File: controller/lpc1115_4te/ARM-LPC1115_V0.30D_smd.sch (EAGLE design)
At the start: 97 parts, among them IC1 LPC1115, IC2 BD9G101, Q2 BCP52, Q3 BC856, Q4 12MHz, T1 BC547C

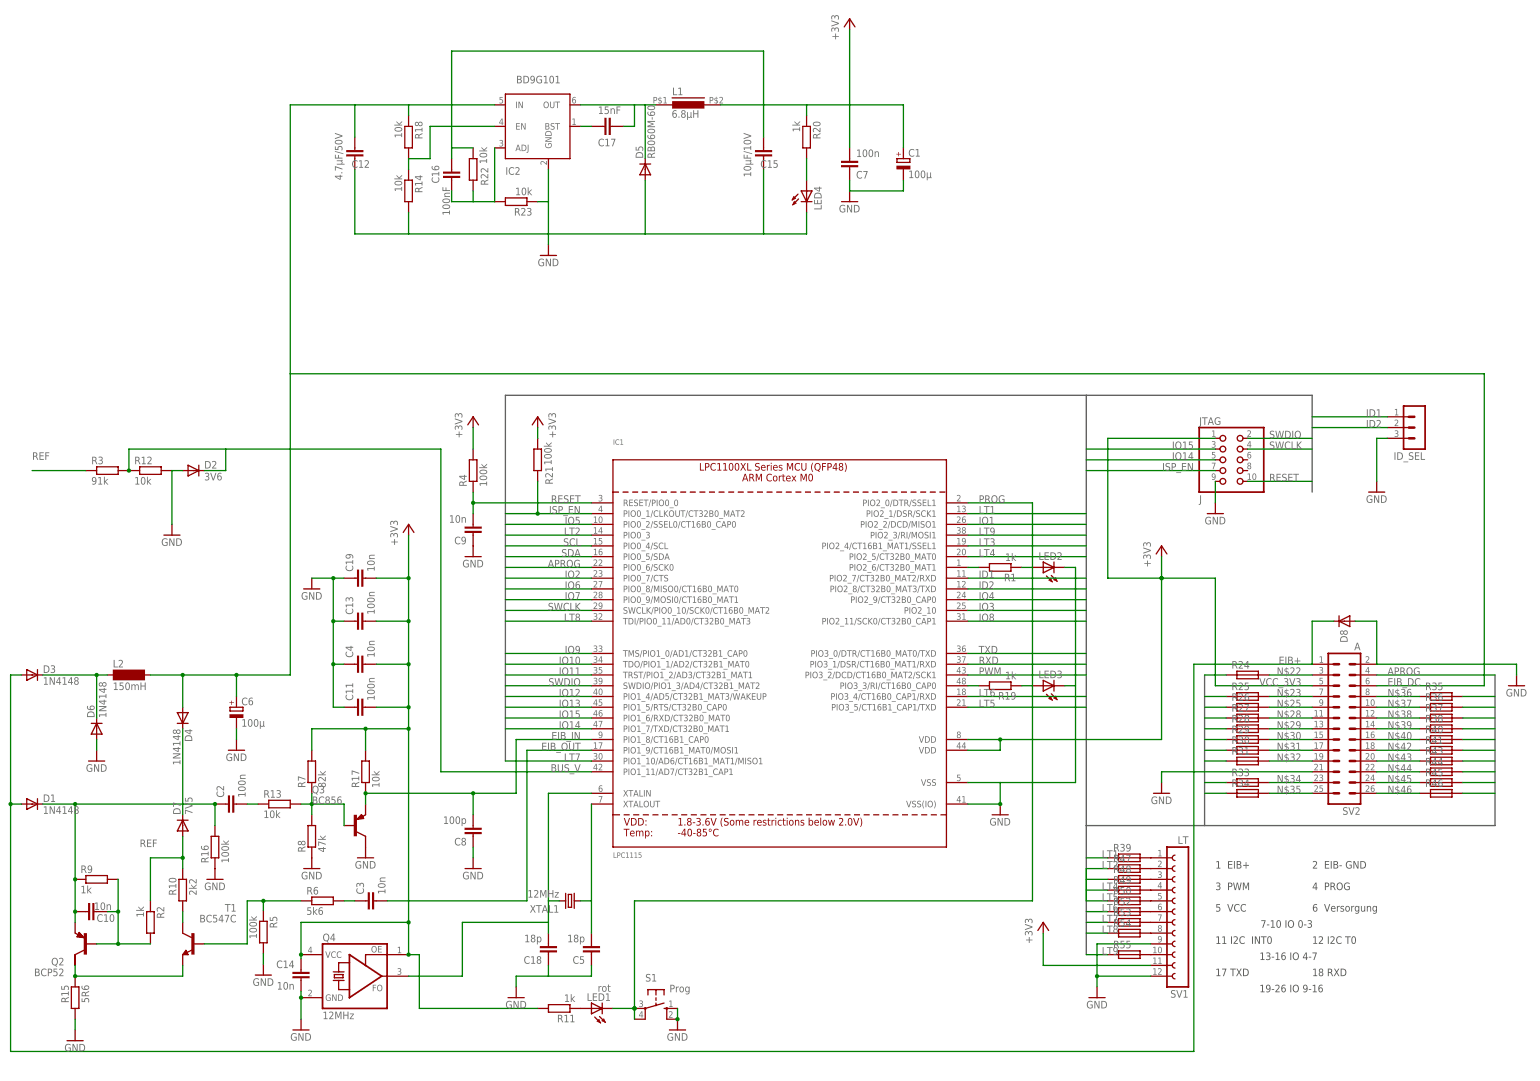
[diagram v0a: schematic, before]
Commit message: Bezeichungen verschoben und Hinweise ergänzt
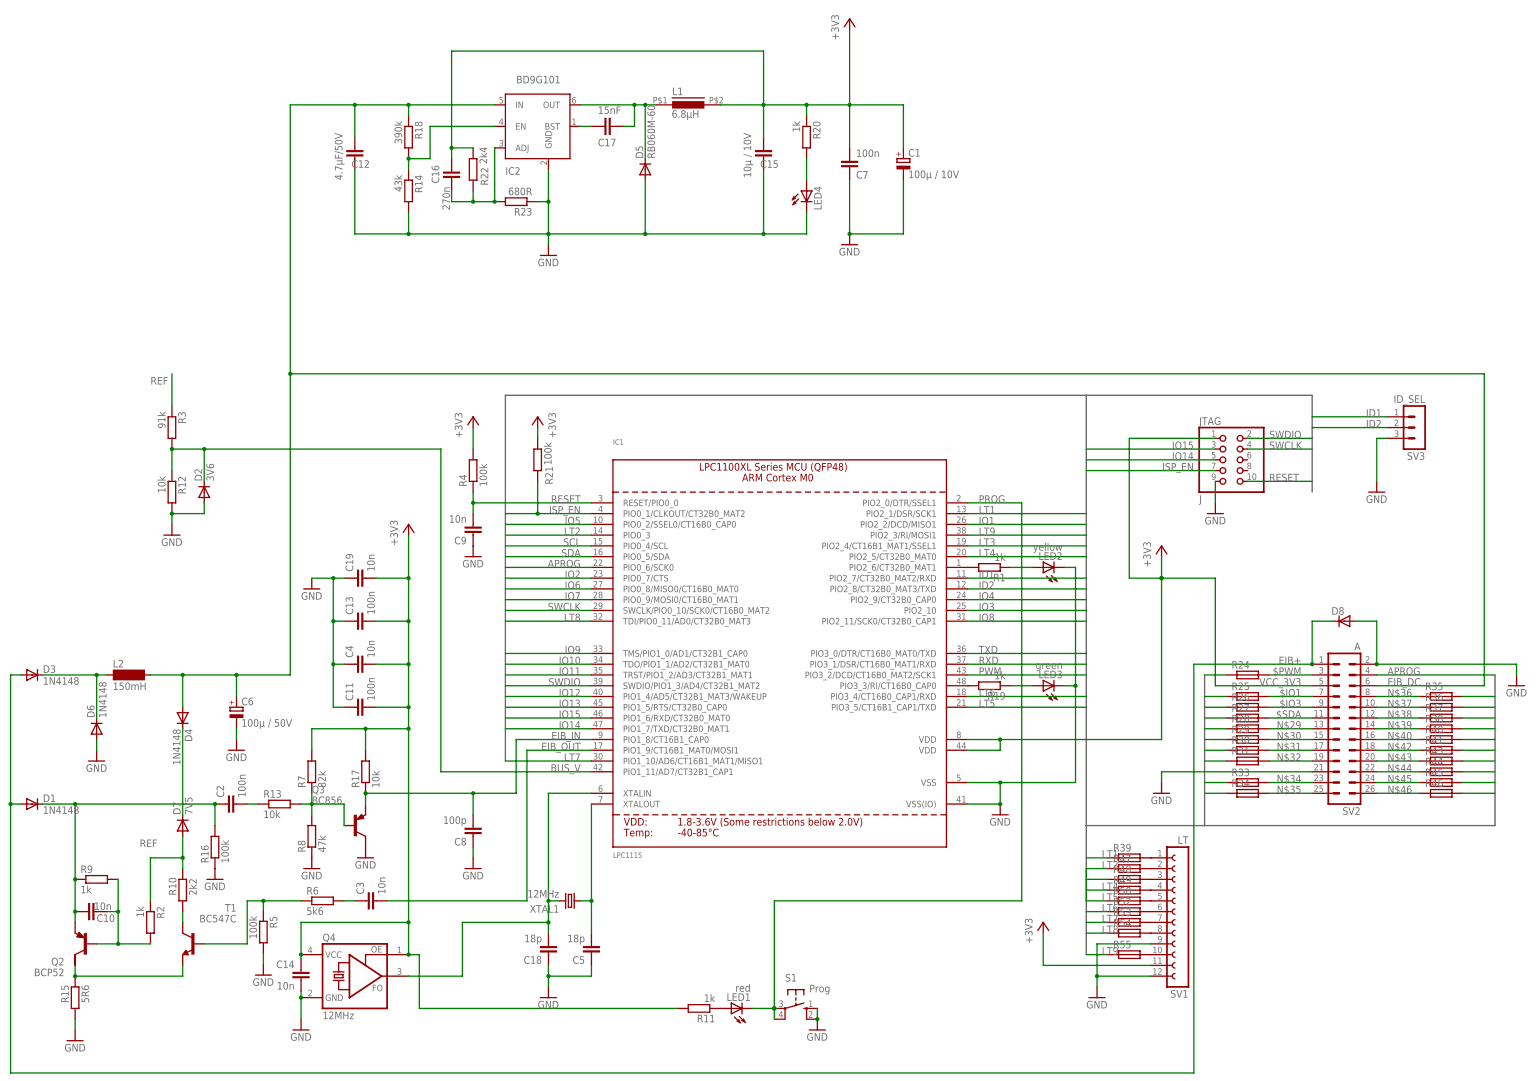
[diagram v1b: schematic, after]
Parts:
- C1: value 100µ -> 100µ / 10V
- C15: value 10µF/10V -> 10µ / 10V
- C16: value 100nF -> 270n
- C6: value 100µ -> 100µ / 50V
- LED1: value rot -> red
- LED2: value (none) -> yellow
- LED3: value (none) -> green
- R14: value 10k -> 43k
- R18: value 10k -> 390k
- R22: value 10k -> 2k4
- R23: value 10k -> 680R
- SV3: value (none) -> ID_SEL
- renumbered ID_SEL to SV3
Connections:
- net N$22 renamed $PWM
- net N$23 renamed $IO1
- net N$25 renamed $IO3
- net N$28 renamed $SDA
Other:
- note added: "C1 kann entfallen wenn die App wenig Strom braucht"
- note added: "D8 mit SMAJ40C bestücken wenn Controller ohne App Platine verwendet wird."
- note added: "Die Schutzwiderstände R24..R55 vor SV1 und SV2 sind optional und sollten nur bei Bedarf bestücken."
- note added: "Power LED (LED4+R20) ist optional"
- note added: "Quarz versus Oszillator: Entweder Oszillator Q4 bestücken oder Quarz XTAL1 mit C5+C18 Nicht beide!"
- note added: "Vorsicht bei R6 und R15: 5R6 nicht mit 5k6 verwechseln (ein beliebter Fehler)"
- note removed: "1 EIB+"
- note removed: "11 I2C INT0"
- note removed: "12 I2C T0"
- note removed: "13-16 IO 4-7"
- note removed: "17 TXD"
- note removed: "18 RXD"
- note removed: "19-26 IO 9-16"
- note removed: "2 EIB- GND"
- note removed: "3 PWM"
- note removed: "4 PROG"
- note removed: "5 VCC"
- note removed: "6 Versorgung"
- note removed: "7-10 IO 0-3"
- moved on the sheet: D2, LED1, R1, R11, R12, R19, R3, S1
